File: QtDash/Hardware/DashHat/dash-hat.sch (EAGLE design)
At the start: 169 parts, among them IC1 LMV614, IC10 MAX9924, IC11 ZXTR2105FQ, IC2 MCP3X083008, IC3 MCP23017SS, IC4 LM358D, IC5 IL300, IC6 TSV912D, IC7 IL300, IC8 TSV912D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

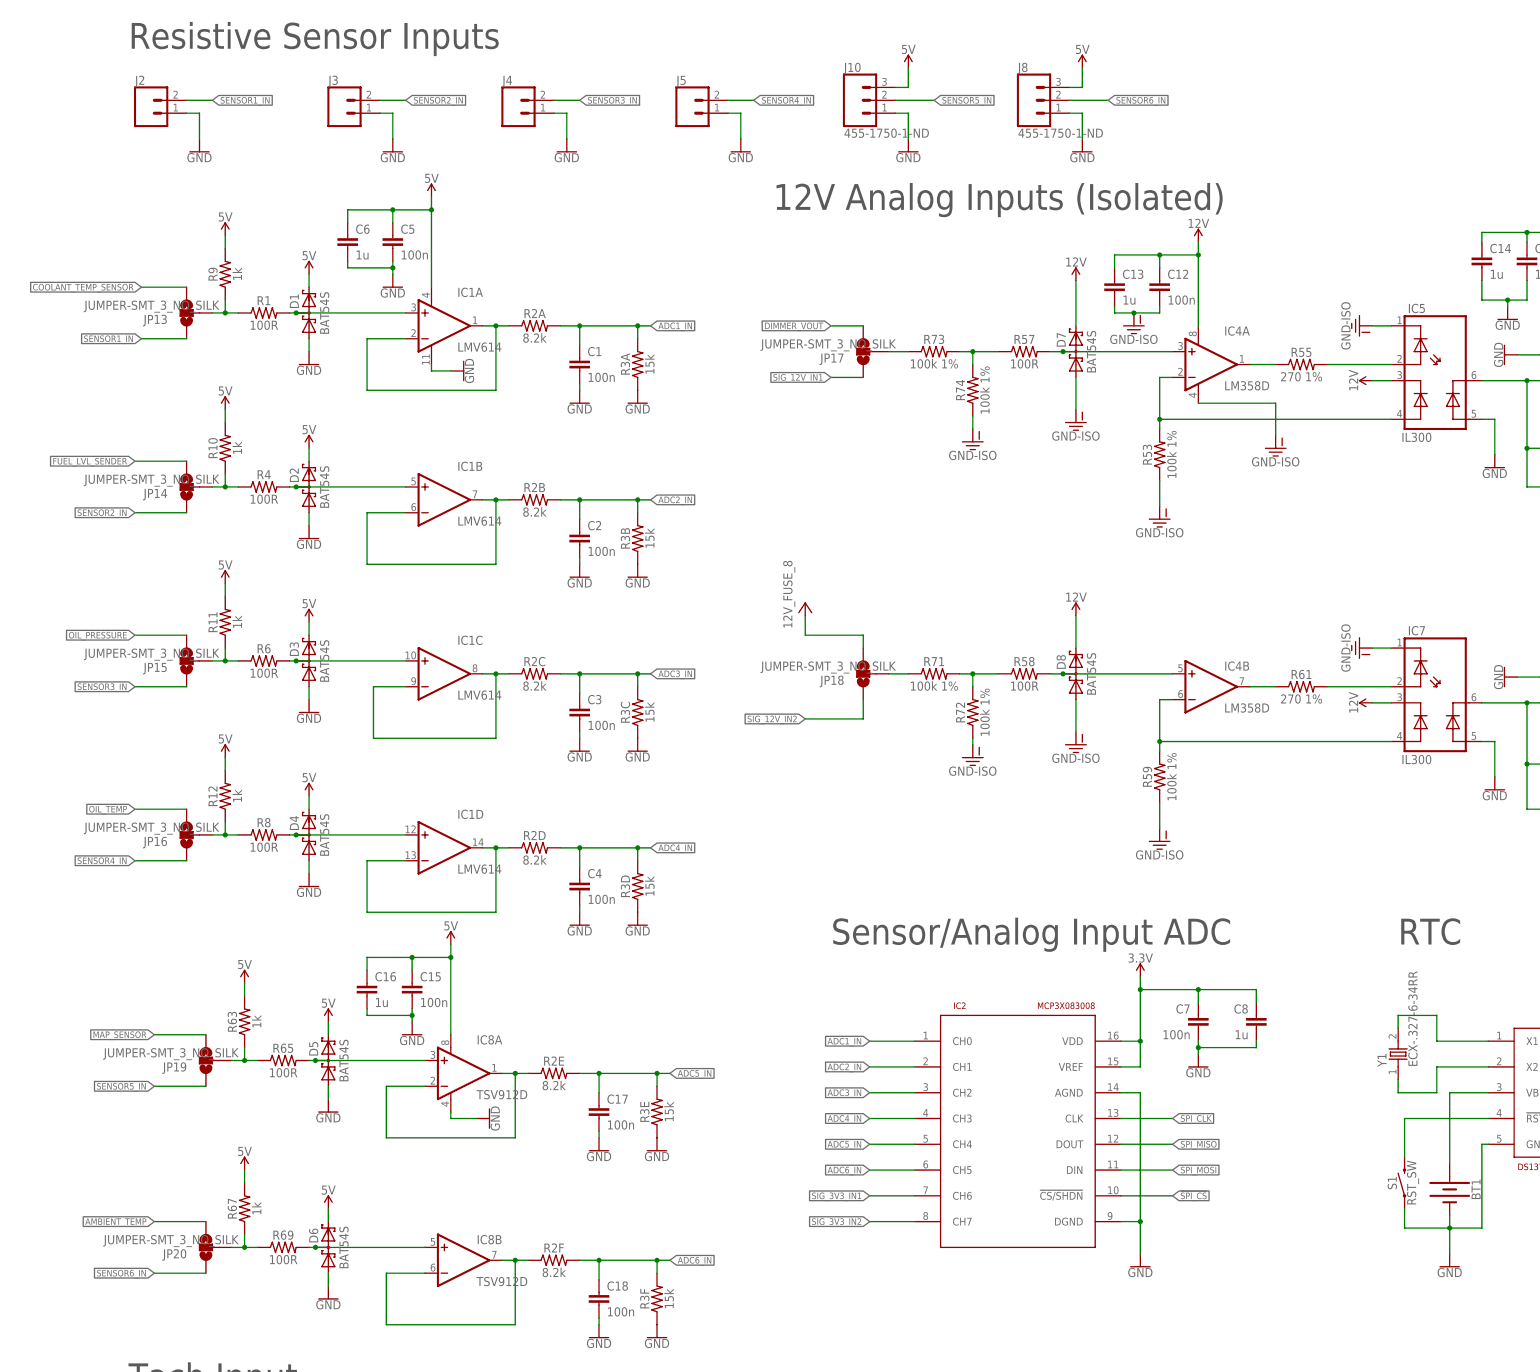
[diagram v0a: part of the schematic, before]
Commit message: topic/hardware-revc: 	- removed individual pin headers for sensor inputs -- changed to molex 8 pin for now, might be too large
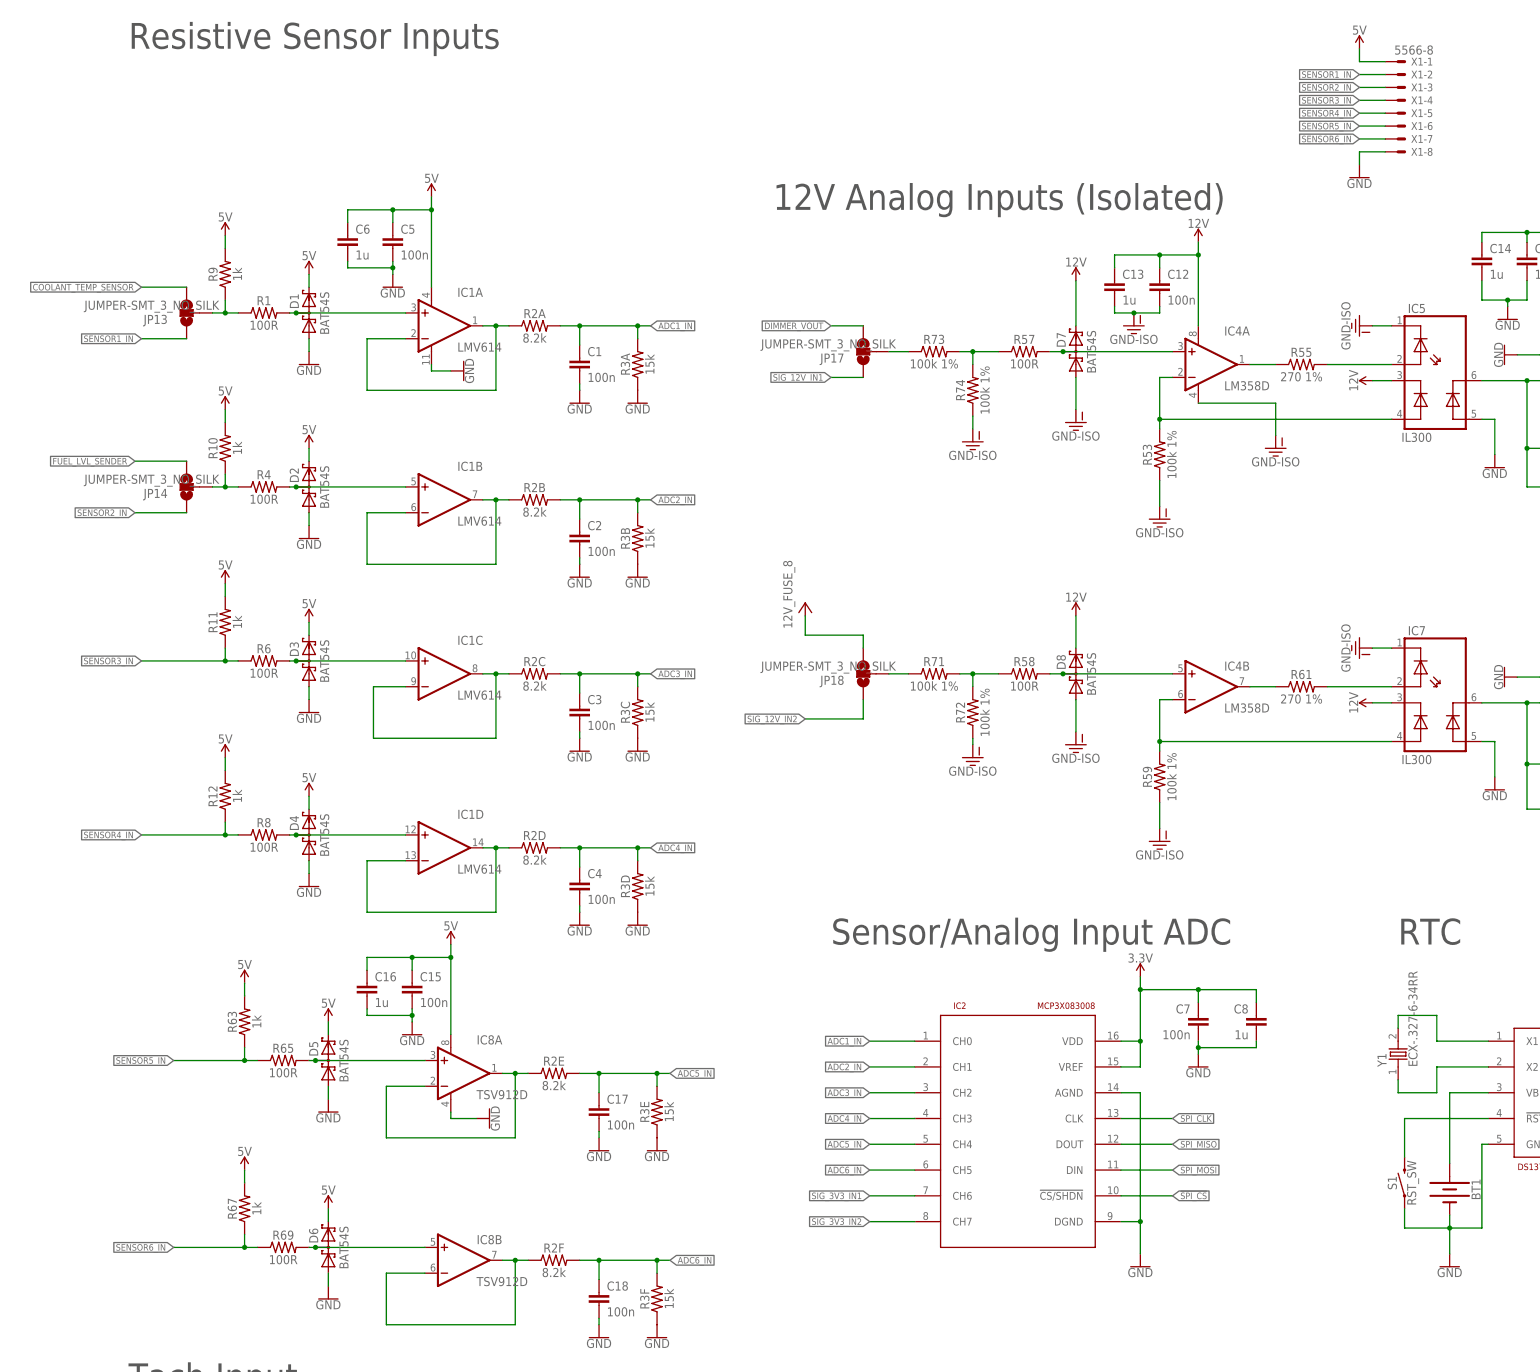
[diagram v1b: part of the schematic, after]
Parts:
- removed J10, J8: 455-1750-1-ND, SparkFun-Connectors:CONN_03
- removed J2, J3, J4, J5: (no value), SparkFun-Connectors:CONN_02
- removed JP15, JP16, JP19, JP20: JUMPER-SMT_3_NO_SILK, SparkFun-Jumpers:JUMPER-SMT_3_NO_SILK
- added X1: 5566-8, con-molex:5566-8
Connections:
- removed net AMBIENT_TEMP: JP20.3
- removed net MAP_SENSOR: JP19.3
- removed net N$30: JP15.2, R11.1, R6.1
- removed net N$31: JP16.2, R12.1, R8.1
- removed net N$34: JP19.2, R63.1, R65.1
- removed net N$37: JP20.2, R67.1, R69.1
- removed net OIL_PRESSURE: JP15.3
- removed net OIL_TEMP: JP16.3
- net 5V: now also X1-1.S; no longer J10.3, J8.3
- net GND: now also X1-8.S; no longer J10.1, J2.1, J3.1, J4.1, J5.1, J8.1
- net SENSOR1_IN: now also X1-2.S; no longer J2.2
- net SENSOR2_IN: now also X1-3.S; no longer J3.2
- net SENSOR3_IN: now also R11.1, R6.1, X1-4.S; no longer J4.2, JP15.1
- net SENSOR4_IN: now also R12.1, R8.1, X1-5.S; no longer J5.2, JP16.1
- net SENSOR5_IN: now also R63.1, R65.1, X1-6.S; no longer J10.2, JP19.1
- net SENSOR6_IN: now also R67.1, R69.1, X1-7.S; no longer J8.2, JP20.1

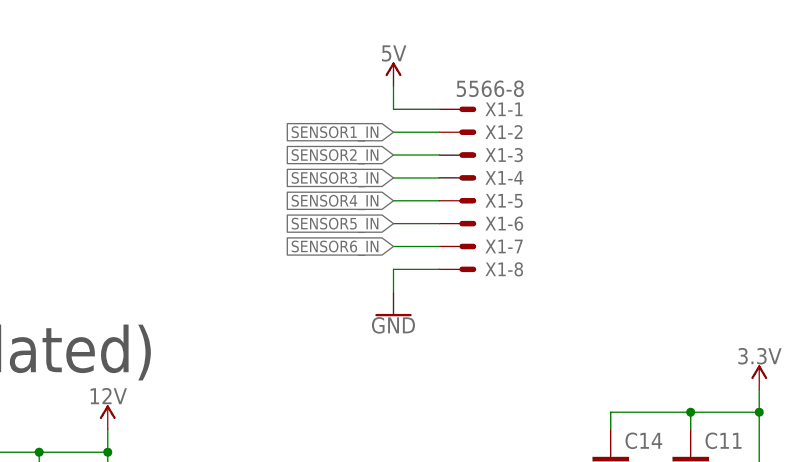
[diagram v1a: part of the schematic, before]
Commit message: topic/hardware-revc: 	- replaced larger molex connector smaller molex connector
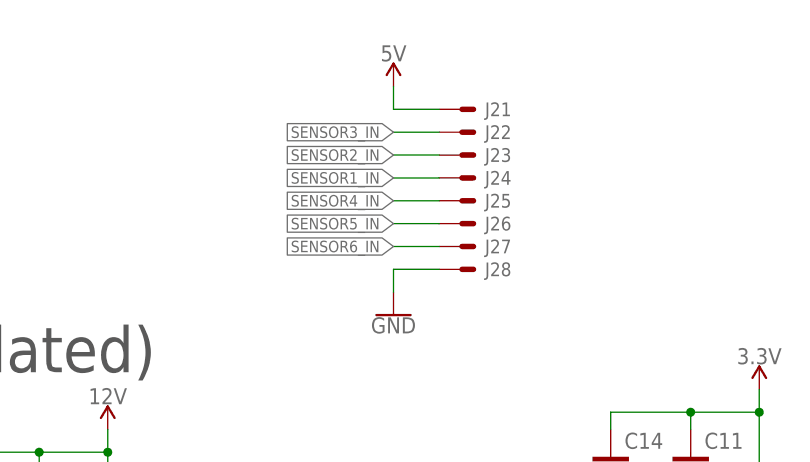
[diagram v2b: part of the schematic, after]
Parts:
- removed X1: 5566-8, con-molex:5566-8
- added J2: CONN_04X2, digital_dash:CONN_04X2
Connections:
- net 5V: now also J21.S; no longer X1-1.S
- net GND: now also J28.S; no longer X1-8.S
- net SENSOR1_IN: now also J24.S; no longer X1-2.S
- net SENSOR2_IN: now also J23.S; no longer X1-3.S
- net SENSOR3_IN: now also J22.S; no longer X1-4.S
- net SENSOR4_IN: now also J25.S; no longer X1-5.S
- net SENSOR5_IN: now also J26.S; no longer X1-6.S
- net SENSOR6_IN: now also J27.S; no longer X1-7.S
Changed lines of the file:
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@@
 <setting verticaltext="up"/>
 </settings>
-<grid distance="0.05" unitdist="inch" unit="inch" style="lines" multiple="1" display="no" altdistance="0.01" altunitdist="inch" altunit="inch"/>
+<grid distance="0.1" unitdist="inch" unit="inch" style="lines" multiple="1" display="no" altdistance="0.01" altunitdist="inch" altunit="inch"/>
 <layers>
 <layer number="1" name="Top" color="4" fill="1" visible="no" active="no"/>
@@
 <part name="SUPPLY61" library="SparkFun-PowerSymbols" deviceset="3.3V" device=""/>
 <part name="GND45" library="SparkFun-PowerSymbols" deviceset="GND" device=""/>
-<part name="X1" library="con-molex" deviceset="5566-8" device=""/>
 <part name="SUPPLY52" library="SparkFun-PowerSymbols" deviceset="5V" device=""/>
 <part name="GND52" library="SparkFun-PowerSymbols" deviceset="GND" device=""/>
+<part name="J2" library="digital_dash" deviceset="CONN_04X2" device=""/>
 </parts>
 <sheets>
@@
 <instance part="SUPPLY61" gate="G$1" x="506.73" y="237.49"/>
 <instance part="GND45" gate="1" x="494.03" y="198.12" rot="MR0"/>
-<instance part="X1" gate="-1" x="279.4" y="414.02"/>
-<instance part="X1" gate="-2" x="279.4" y="411.48"/>
-<instance part="X1" gate="-3" x="279.4" y="408.94"/>
-<instance part="X1" gate="-4" x="279.4" y="406.4"/>
-<instance part="X1" gate="-5" x="279.4" y="403.86"/>
-<instance part="X1" gate="-6" x="279.4" y="401.32"/>
-<instance part="X1" gate="-7" x="279.4" y="398.78"/>
-<instance part="X1" gate="-8" x="279.4" y="396.24"/>
 <instance part="SUPPLY52" gate="G$1" x="271.78" y="416.56"/>
 <instance part="GND52" gate="1" x="271.78" y="391.16"/>
+<instance part="J2" gate="1" x="279.4" y="414.02"/>
+<instance part="J2" gate="2" x="279.4" y="411.48"/>
+<instance part="J2" gate="3" x="279.4" y="408.94"/>
+<instance part="J2" gate="4" x="279.4" y="406.4"/>
+<instance part="J2" gate="5" x="279.4" y="403.86"/>
+<instance part="J2" gate="6" x="279.4" y="401.32"/>
+<instance part="J2" gate="7" x="279.4" y="398.78"/>
+<instance part="J2" gate="8" x="279.4" y="396.24"/>
 </instances>
 <busses>
@@
 </segment>
 <segment>
-<pinref part="X1" gate="-2" pin="S"/>
-<wire x1="276.86" y1="411.48" x2="271.78" y2="411.48" width="0.1524" layer="91"/>
-<label x="271.78" y="411.48" size="1.27" layer="95" rot="R180" xref="yes"/>
+<pinref part="J2" gate="4" pin="S"/>
+<wire x1="276.86" y1="406.4" x2="271.78" y2="406.4" width="0.1524" layer="91"/>
+<label x="271.78" y="406.4" size="1.27" layer="95" rot="R180" xref="yes"/>
 </segment>
 </net>
@@
 </segment>
 <segment>
-<pinref part="X1" gate="-3" pin="S"/>
+<pinref part="J2" gate="3" pin="S"/>
 <wire x1="276.86" y1="408.94" x2="271.78" y2="408.94" width="0.1524" layer="91"/>
 <label x="271.78" y="408.94" size="1.27" layer="95" rot="R180" xref="yes"/>
@@
 </segment>
 <segment>
-<pinref part="X1" gate="-4" pin="S"/>
-<wire x1="276.86" y1="406.4" x2="271.78" y2="406.4" width="0.1524" layer="91"/>
-<label x="271.78" y="406.4" size="1.27" layer="95" rot="R180" xref="yes"/>
+<pinref part="J2" gate="2" pin="S"/>
+<wire x1="276.86" y1="411.48" x2="271.78" y2="411.48" width="0.1524" layer="91"/>
+<label x="271.78" y="411.48" size="1.27" layer="95" rot="R180" xref="yes"/>
 </segment>
 </net>
@@
 </segment>
 <segment>
-<pinref part="X1" gate="-5" pin="S"/>
 <wire x1="276.86" y1="403.86" x2="271.78" y2="403.86" width="0.1524" layer="91"/>
 <label x="271.78" y="403.86" size="1.27" layer="95" rot="R180" xref="yes"/>
+<pinref part="J2" gate="5" pin="S"/>
 </segment>
 </net>
@@
 </segment>
 <segment>
-<pinref part="X1" gate="-8" pin="S"/>
 <wire x1="276.86" y1="396.24" x2="271.78" y2="396.24" width="0.1524" layer="91"/>
 <wire x1="271.78" y1="396.24" x2="271.78" y2="393.7" width="0.1524" layer="91"/>
 <pinref part="GND52" gate="1" pin="GND"/>
+<pinref part="J2" gate="8" pin="S"/>
 </segment>
 </net>
@@
 </segment>
 <segment>
-<pinref part="X1" gate="-1" pin="S"/>
 <pinref part="SUPPLY52" gate="G$1" pin="5V"/>
 <wire x1="276.86" y1="414.02" x2="271.78" y2="414.02" width="0.1524" layer="91"/>
 <wire x1="271.78" y1="414.02" x2="271.78" y2="416.56" width="0.1524" layer="91"/>
+<pinref part="J2" gate="1" pin="S"/>
 </segment>
 </net>
@@
 </segment>
 <segment>
-<pinref part="X1" gate="-6" pin="S"/>
 <wire x1="276.86" y1="401.32" x2="271.78" y2="401.32" width="0.1524" layer="91"/>
 <label x="271.78" y="401.32" size="1.27" layer="95" rot="R180" xref="yes"/>
+<pinref part="J2" gate="6" pin="S"/>
 </segment>
 </net>
@@
 </segment>
 <segment>
-<pinref part="X1" gate="-7" pin="S"/>
 <wire x1="276.86" y1="398.78" x2="271.78" y2="398.78" width="0.1524" layer="91"/>
 <label x="271.78" y="398.78" size="1.27" layer="95" rot="R180" xref="yes"/>
+<pinref part="J2" gate="7" pin="S"/>
 </segment>
 </net>
